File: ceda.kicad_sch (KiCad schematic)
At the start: 0 parts

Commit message: CTC, serial clock and main clock
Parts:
- added C52, C53, C54: C, symbol Device:C
- added J4: MAINCLK, symbol ceda:MAINCLK
- added K15, UA7: 74LS04, symbol 74xx:74LS04
- added R56: R, symbol Device:R
- added UA6: 74LS161, symbol 74xx:74LS161
- added XTAL3: 16M, symbol Device:Crystal
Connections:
- new net: J4.4 (B1), UA6.13 (Q1), UA7.11, UA7.13
- new net: J4.2 (A1), UA6.14 (Q0)
- new net: K15.6, UA6.2 (CP)
- new net: UA6.3 (D0), UA6.4 (D1), UA6.5 (D2), UA6.6 (D3)
- new net: C52.1, C54.2, K15.3, R56.2
- new net: J4.3 (B0), UA7.5
- new net: C54.1, XTAL3.1
- new net: C53.1, K15.4, K15.5, R56.1, XTAL3.2
- new net +5V: C52.2, C53.2, UA6.1 (~{MR}), UA6.9 (~{PE})
- new net FDC_CLK: UA7.6
- new net main clock: UA7.12
- no-connect marks 0 -> 1
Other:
- added sheet CTC (ctc.kicad_sch)

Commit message: Schematics refactoring:
- New sheet reserved to video memory.
- Removed video memory parts inside video_generation.
- Removed video memory parts inside GPIO.
- Generic cleanup to keep all circuits inside each sheet.
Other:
- sheet SERIAL renamed Serial
- sheet Speaker renamed IO space
- added sheet Video Memory (video_memory.kicad_sch)
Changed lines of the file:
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@@
     )
   )
-  (sheet (at 25.4 54.61) (size 29.21 21.59) (fields_autoplaced)
+  (sheet (at 214.63 54.61) (size 29.21 21.59) (fields_autoplaced)
     (stroke (width 0.1524) (type solid))
     (fill (color 0 0 0 0.0000))
-    (property "Sheetname" "GPIO" (at 25.4 53.8984 0)
+    (property "Sheetname" "GPIO" (at 214.63 53.8984 0)
       (effects (font (size 1.27 1.27)) (justify left bottom))
     )
-    (property "Sheetfile" "GPIO.kicad_sch" (at 25.4 76.7846 0)
+    (property "Sheetfile" "GPIO.kicad_sch" (at 214.63 76.7846 0)
       (effects (font (size 1.27 1.27)) (justify left top))
     )
@@
       (project "ceda"
         (path "/12a6dbe3-008d-4c5b-88f6-9f1c816060be" (page "11"))
+      )
+    )
+  )
+  (sheet (at 25.4 54.61) (size 29.21 21.59) (fields_autoplaced)
+    (stroke (width 0.1524) (type solid))
+    (fill (color 0 0 0 0.0000))
+    (property "Sheetname" "Video Memory" (at 25.4 53.8984 0)
+      (effects (font (size 1.27 1.27)) (justify left bottom))
+    )
+    (property "Sheetfile" "video_memory.kicad_sch" (at 25.4 76.7846 0)
+      (effects (font (size 1.27 1.27)) (justify left top))
+    )
+    (instances
+      (project "ceda"
+        (path "/12a6dbe3-008d-4c5b-88f6-9f1c816060be" (page "13"))
       )
     )
@@
     (stroke (width 0.1524) (type solid))
     (fill (color 0 0 0 0.0000))
-    (property "Sheetname" "SERIAL" (at 63.5 24.6884 0)
+    (property "Sheetname" "Serial" (at 63.5 24.6884 0)
       (effects (font (size 1.27 1.27)) (justify left bottom))
     )
@@
     (stroke (width 0.1524) (type solid))
     (fill (color 0 0 0 0.0000))
-    (property "Sheetname" "Speaker" (at 101.6 24.6884 0)
+    (property "Sheetname" "IO space" (at 101.6 24.6884 0)
       (effects (font (size 1.27 1.27)) (justify left bottom))
     )

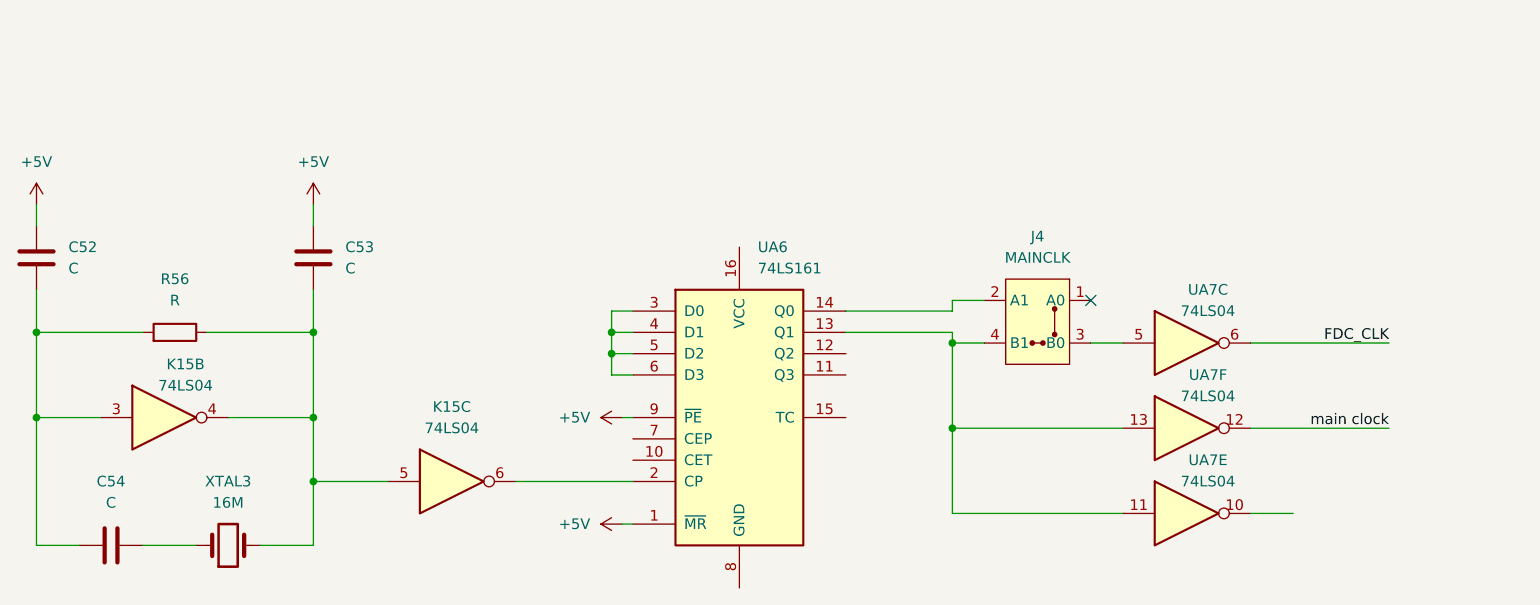
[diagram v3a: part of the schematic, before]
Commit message: Moved clock circuit in the clock/reset sheet
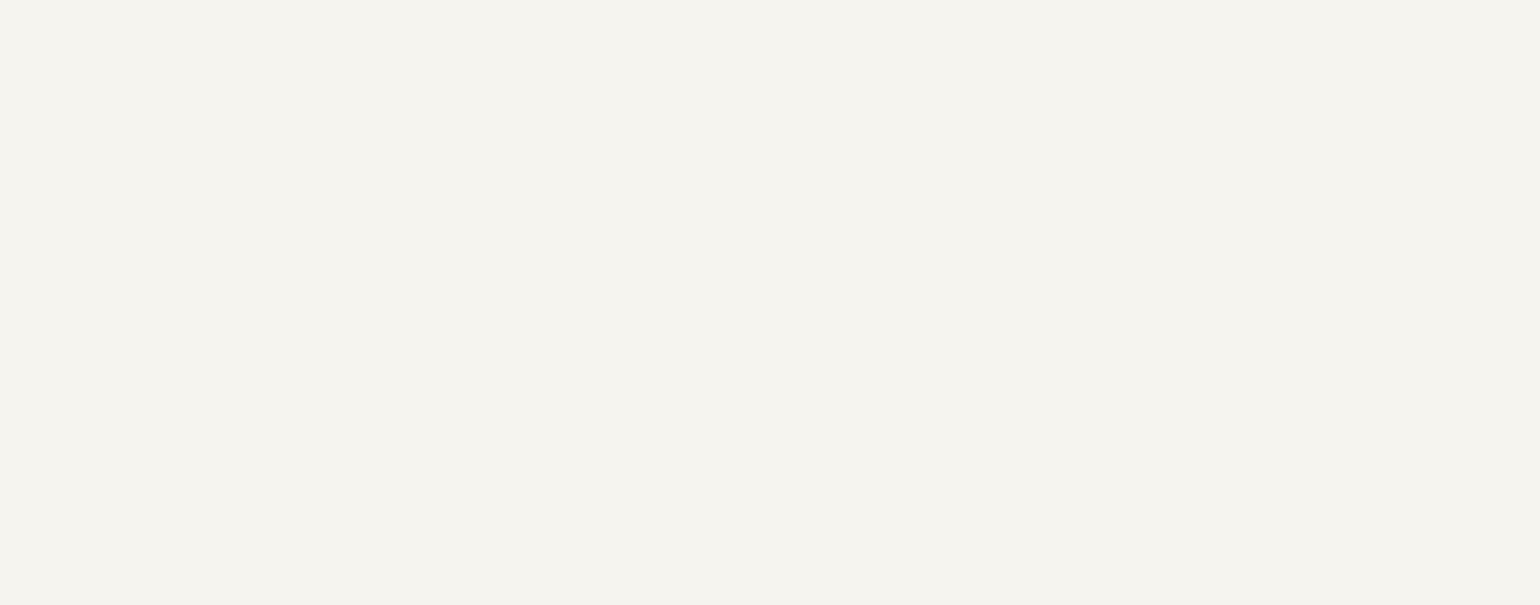
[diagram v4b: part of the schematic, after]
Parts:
- removed C52, C53, C54: C, symbol Device:C
- removed J4: MAINCLK, symbol ceda:MAINCLK
- removed K15, UA7: 74LS04, symbol 74xx:74LS04
- removed R56: R, symbol Device:R
- removed UA6: 74LS161, symbol 74xx:74LS161
- removed XTAL3: 16M, symbol Device:Crystal
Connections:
- no-connect marks 1 -> 0

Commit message: Notes in kicad's sheet text blocks
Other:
- title: FPX-290 -> CEDA - Sanco 8003 schematics
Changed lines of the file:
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@@
   (paper "A4")
   (title_block
-    (title "FPX-290")
+    (title "CEDA - Sanco 8003 schematics")
     (rev "05")
     (company "Logic Systems Int'l Inc")
+    (comment 1 "reversed by RetrOfficina - retrofficina.glgprograms.it")
   )
   (text "These schematics have been reverse engineered from a Sanco 8003.\n\nThis is a work in progress. Beware of mistakes. No warranty.\n\nDownload the latest version, consider contributing, and report issues at:\ngithub.com/GLGPrograms/ceda-schematics\nretrofficina.glgprograms.it\n"

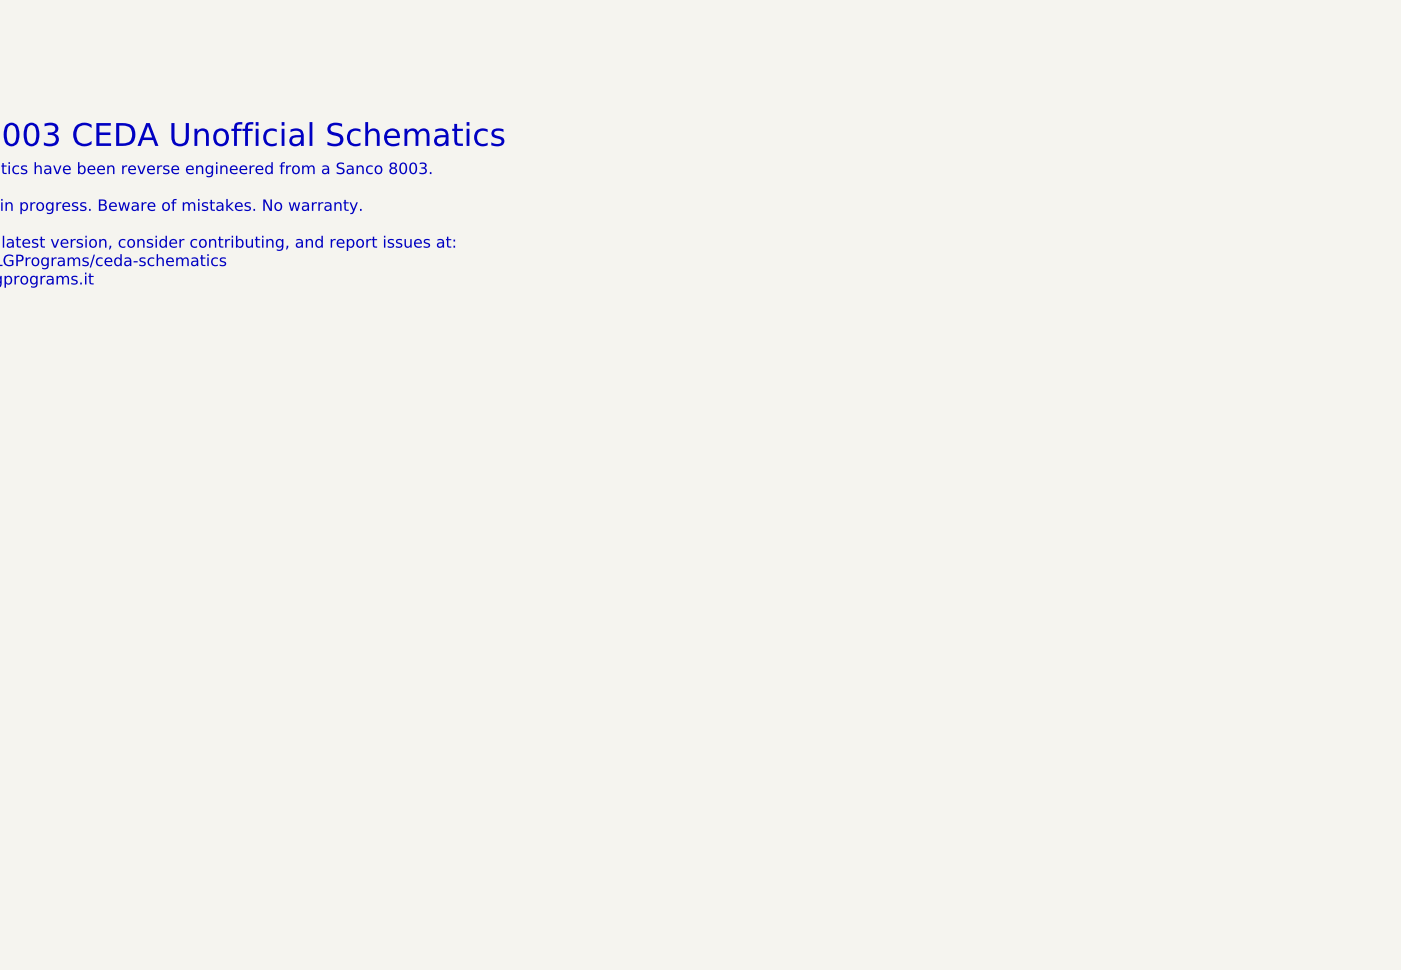
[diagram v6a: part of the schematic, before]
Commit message: pcb: added all the connector, 99% routed
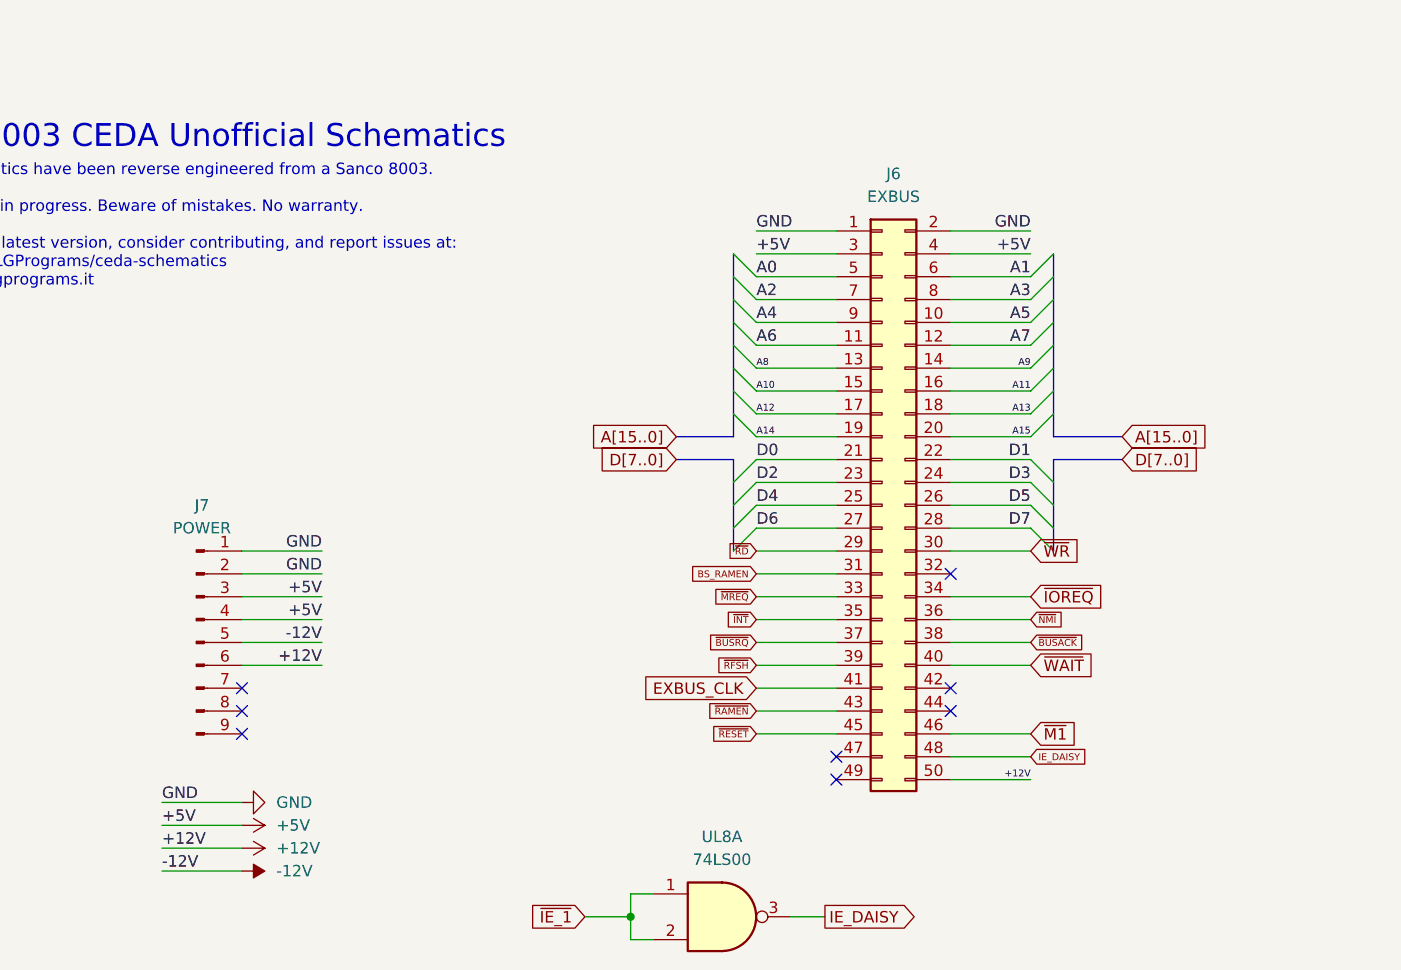
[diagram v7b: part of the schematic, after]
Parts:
- added J6: EXBUS, Connector_IDC:IDC-Header_2x25_P2.54mm_Vertical, symbol Connector_Generic:Conn_02x25_Odd_Even
- added J7: POWER, TerminalBlock_CUI:TerminalBlock_CUI_TB007-508-09_1x09_P5.08mm_Horizontal, symbol Connector:Conn_01x09_Pin
- added UL8: 74LS00, Package_DIP:DIP-14_W7.62mm, symbol 74xx:74LS00
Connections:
- new net +12V: J6.50 (Pin_50), J7.6 (Pin_6)
- new net +5V: J6.3 (Pin_3), J6.4 (Pin_4), J7.3 (Pin_3), J7.4 (Pin_4)
- new net -12V: J7.5 (Pin_5)
- new net A0: J6.5 (Pin_5)
- new net A1: J6.6 (Pin_6)
- new net A10: J6.15 (Pin_15)
- new net A11: J6.16 (Pin_16)
- new net A12: J6.17 (Pin_17)
- new net A13: J6.18 (Pin_18)
- new net A14: J6.19 (Pin_19)
- new net A15: J6.20 (Pin_20)
- new net A2: J6.7 (Pin_7)
- new net A3: J6.8 (Pin_8)
- new net A4: J6.9 (Pin_9)
- new net A5: J6.10 (Pin_10)
- new net A6: J6.11 (Pin_11)
- new net A7: J6.12 (Pin_12)
- new net A8: J6.13 (Pin_13)
- new net A9: J6.14 (Pin_14)
- new net BS_RAMEN: J6.31 (Pin_31)
- new net D0: J6.21 (Pin_21)
- new net D1: J6.22 (Pin_22)
- new net D2: J6.23 (Pin_23)
- new net D3: J6.24 (Pin_24)
- new net D4: J6.25 (Pin_25)
- new net D5: J6.26 (Pin_26)
- new net D6: J6.27 (Pin_27)
- new net D7: J6.28 (Pin_28)
- new net EXBUS_CLK: J6.41 (Pin_41)
- new net GND: J6.1 (Pin_1), J6.2 (Pin_2), J7.1 (Pin_1), J7.2 (Pin_2)
- new net IE_DAISY: J6.48 (Pin_48), UL8.3
- new net ~{BUSACK}: J6.38 (Pin_38)
- new net ~{BUSRQ}: J6.37 (Pin_37)
- new net ~{IE_1}: UL8.1, UL8.2
- new net ~{INT}: J6.35 (Pin_35)
- new net ~{IOREQ}: J6.34 (Pin_34)
- new net ~{M1}: J6.46 (Pin_46)
- new net ~{MREQ}: J6.33 (Pin_33)
- new net ~{NMI}: J6.36 (Pin_36)
- new net ~{RAMEN}: J6.43 (Pin_43)
- new net ~{RD}: J6.29 (Pin_29)
- new net ~{RESET}: J6.45 (Pin_45)
- new net ~{RFSH}: J6.39 (Pin_39)
- new net ~{WAIT}: J6.40 (Pin_40)
- new net ~{WR}: J6.30 (Pin_30)
- no-connect marks 0 -> 8

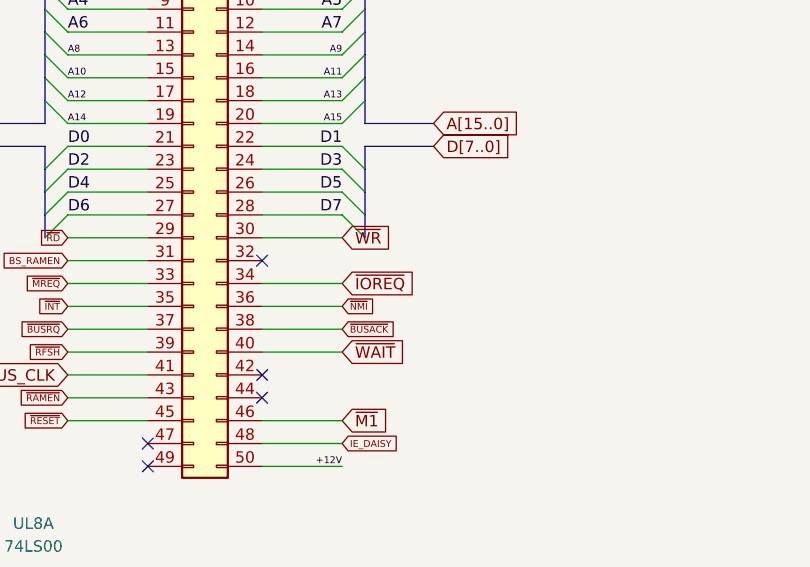
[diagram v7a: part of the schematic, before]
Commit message: pcb and sch: finished routing and fixing connections
There are still some minor inconsistencies (/WR, /RD, one PRINTER
signal), some passives missing (decoupling caps, power stage), but the
schematic and the pcb should be more or less complete.
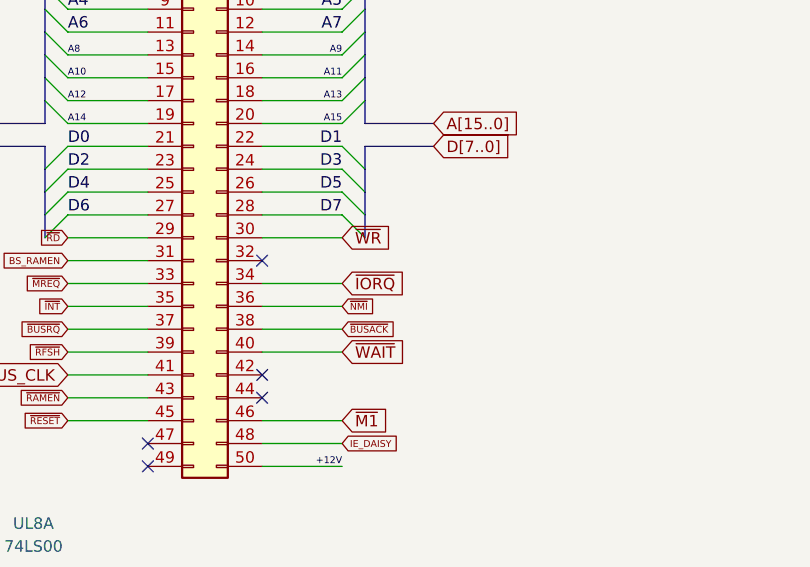
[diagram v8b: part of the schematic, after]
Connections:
- net ~{IOREQ} renamed ~{IORQ}
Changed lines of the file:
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@@
 		)
 	)
-	(global_label "~{IOREQ}"
+	(global_label "~{IORQ}"
 		(shape input)
 		(at 153.67 151.13 0)
@@
 		)
 		(property "Intersheetrefs" "${INTERSHEET_REFS}"
-			(at 162.34 151.13 0)
+			(at 161.191 151.13 0)
 			(effects
 				(font
